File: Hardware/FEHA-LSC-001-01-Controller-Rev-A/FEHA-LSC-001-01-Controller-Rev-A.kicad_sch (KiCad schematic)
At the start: 0 parts

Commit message: LSC: project library parts, schematic capture in progress
Library (_FEHA-LSC-001):
- Imported SI2356DS-T1-GE3, TPS560430XFDBVR, FXL0420-100-M, HDGC4001SMD-S-2P from LCSC;
  ESP32-C3-MINI-1-H4X(4MB) copied from GeyserSense. Fields filled, pin types normalised,
  pins<->pads verified (buck and MOSFET pinouts checked against vendor PDFs)
- TPS560430 symbol pins rearranged by function (VIN/EN left, CB/SW/FB right, GND bottom)

Schematic: reverse-polarity stage, buck (51k/22k divider, 2x10uF 50V input) and MCU core
drawn; BOM fields (Mfr. Part #, LCSC Part #, Package) filled on all placed parts.
Field pass proven electrically neutral with design_diff.py.

Spec BOM: white status LED (C34499) and button (C720477), as GeyserSense.

Co-Authored-By: Claude Opus 5.5 <noreply@anthropic.com>
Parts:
- added C1, C6, C7: 100nF, PCM_JLCPCB:C_0402, symbol PCM_JLCPCB-Capacitors:0402,100nF
- added C2: 1uF, PCM_JLCPCB:C_0402, symbol PCM_JLCPCB-Capacitors:0402,1uF
- added C3, C8: 10uF, PCM_JLCPCB:C_1206, symbol PCM_JLCPCB-Capacitors:1206,10uF
- added C4: 10uF, PCM_JLCPCB:C_0603, symbol PCM_JLCPCB-Capacitors:0603,10uF,(2)
- added C5: 22uF, PCM_JLCPCB:C_1206, symbol PCM_JLCPCB-Capacitors:1206,22uF,(2)
- added CN1: HDGC4001SMD-S-2P, _FEHA-LSC-001:CONN-SMD_2P-P4.00_HDGC4001SMD-S-2P, symbol _FEHA-LSC-001:HDGC4001SMD-S-2P
- added D1: SS34, PCM_JLCPCB:D_SMA, symbol PCM_JLCPCB-Diodes:Schottky,SS34
- added D2: SMBJ26A, PCM_JLCPCB:D_SMB, symbol PCM_JLCPCB-Diodes:TVS-Uni,SMBJ26A
- added D3: White, PCM_JLCPCB:D_0805, symbol PCM_JLCPCB-Diodes:LED,0805,White
- added D4: B5819W SL, PCM_JLCPCB:D_SOD-123, symbol PCM_JLCPCB-Diodes:Schottky,B5819W SL
- added D5: BZT52C10, PCM_JLCPCB:D_SOD-123, symbol PCM_JLCPCB-Diodes:Zener,BZT52C10
- added L1: 10uH, _FEHA-LSC-001:IND-SMD_L4.4-W4.2, symbol _FEHA-LSC-001:FXL0420-100-M
- added Q1: HL2310A, PCM_JLCPCB:Q_SOT-23, symbol PCM_JLCPCB-Transistors:NMOS,HL2310A
- added R1, R2, R4, R8: 10kΩ, PCM_JLCPCB:R_0402, symbol PCM_JLCPCB-Resistors:0402,10kΩ
- added R3: 100kΩ, PCM_JLCPCB:R_0402, symbol PCM_JLCPCB-Resistors:0402,100kΩ
- added R5: 51kΩ, PCM_JLCPCB:R_0402, symbol PCM_JLCPCB-Resistors:0402,51kΩ
- added R6: 22kΩ, PCM_JLCPCB:R_0402, symbol PCM_JLCPCB-Resistors:0402,22kΩ
- added R7: 470Ω, PCM_JLCPCB:R_0402, symbol PCM_JLCPCB-Resistors:0402,470Ω
- added S1: Tactile Button, 160gf, PCM_JLCPCB:SW_TS-1088-AR02016, symbol PCM_JLCPCB-Connectors_Buttons:Tactile Button, 160gf, 12V, 50mA, 4.0mm
- added TP1: GND, TestPoint:TestPoint_Pad_D1.5mm, symbol Connector:TestPoint_Small
- added TP3: EN, TestPoint:TestPoint_Pad_D1.5mm, symbol Connector:TestPoint_Small
- added TP4: VIN, TestPoint:TestPoint_Pad_D1.5mm, symbol Connector:TestPoint_Small
- added U1: TPS560430XFDBVR, _FEHA-LSC-001:SOT-23-6_L2.9-W1.6-P0.95-LS2.8-BR, symbol _FEHA-LSC-001:TPS560430XFDBVR
- added U2: ESP32-C3-MINI-1-H4X(4MB), _FEHA-LSC-001:WIFIM-SMD_ESP32-C3-MINI-1, symbol _FEHA-LSC-001:ESP32-C3-MINI-1-H4X(4MB)
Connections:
- new net: C7.1, U1.1 (CB)
- new net: D3.2, R7.2
- new net +24V: C3.1, C8.1, CN1.1, D2.1, R3.1, U1.4 (EN), U1.5 (VIN)
- new net +3V3: C4.1, C5.1, C6.1, L1.1, R1.1, R2.1, R4.1, R5.1, R8.1, U2.3 (3V3)
- new net BTN: C1.1, R1.2, S1.1 (A), U2.23 (IO9)
- new net EN: C2.1, R8.2, TP3.1, U2.8 (EN)
- new net FB: R5.2, R6.1, U1.3 (FB)
- new net GND: C1.2, C2.2, C3.2, C4.2, C5.2, C6.2, C8.2, D2.2, D3.1, D5.2, Q1.2 (S), R6.2, S1.2 (B), TP1.1, U1.2 (GND), U2.1 (GND), U2.11 (GND), U2.14 (GND), U2.2 (GND), U2.36 (GND), U2.37 (GND), U2.38 (GND), U2.39 (GND), U2.40 (GND), U2.41 (GND), U2.42 (GND), U2.43 (GND), U2.44 (GND), U2.45 (GND), U2.46 (GND), U2.47 (GND), U2.48 (GND), U2.49 (GND), U2.50 (GND), U2.51 (GND), U2.52 (GND), U2.53 (GND)
- new net G_REV: D5.1, Q1.1 (G), R3.2
- new net IO2: R4.2, U2.5 (IO2)
- new net IO8: R2.2, U2.22 (IO8)
- new net LED_USER: R7.1, U2.16 (IO10)
- new net SW: C7.2, L1.2, U1.6 (SW)
- new net VBUS: D4.2
- new net VIN_N: CN1.2, Q1.3 (D)
- no-connect marks 0 -> 5
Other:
- note added: "Microprocessor"

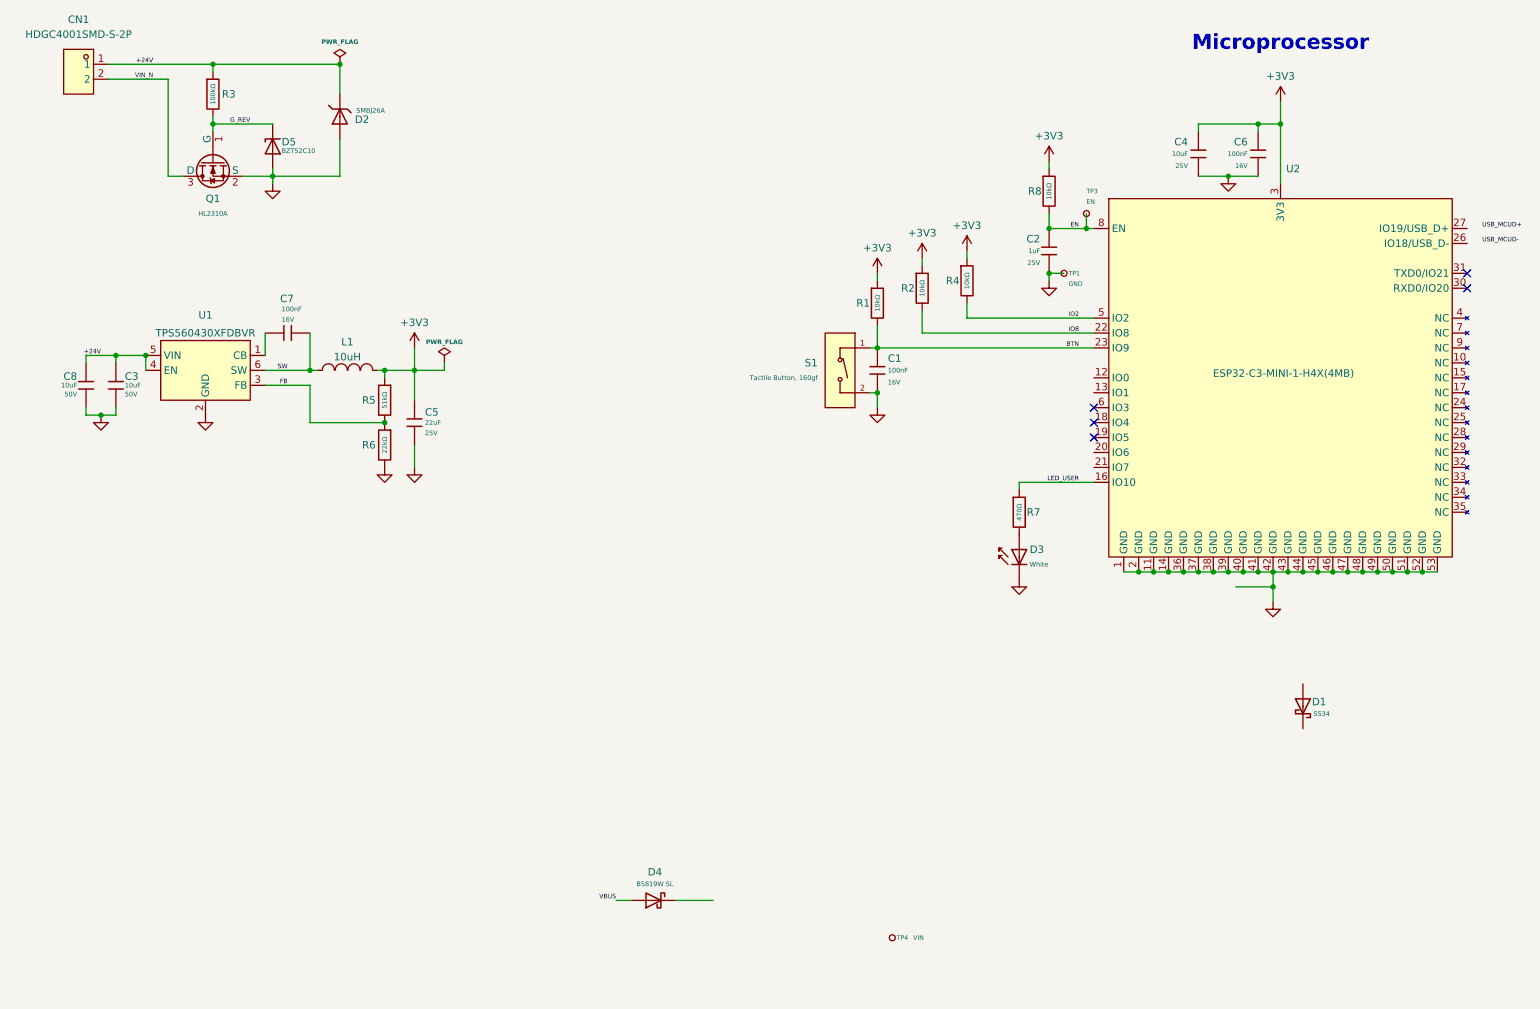
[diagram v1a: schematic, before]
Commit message: LSC: output stage, USB debug header, PWR_1A net class
- Output stage: SI2356DS low-side switch (100R gate series, 10k pull-down), SS34
  freewheel, 1uF 50V 0805 local bypass (C28323), drain test point TP6 + GND TP7
- CN3 USB debug header (VBUS, D-, D+, GND) on new locking footprint
  PinHeader_1x04_P2.54mm_Vertical_Lock (holes staggered +-0.127 mm for an unsoldered
  press-fit header); USB_MCUD+/- wired to U2 IO19/IO18
- Removed the two net-class flags carried over from GeyserSense; new net class PWR_1A
  (1.0 mm track) on /+24V, /VIN_N, /LED_N, GND (spec §7 rule 6)
- BOM fields filled on C10 and R10; flag removal proven neutral with design_diff.py.
  ERC clean apart from kicad-cli library-path warnings

Co-Authored-By: Claude Opus 5.5 <noreply@anthropic.com>
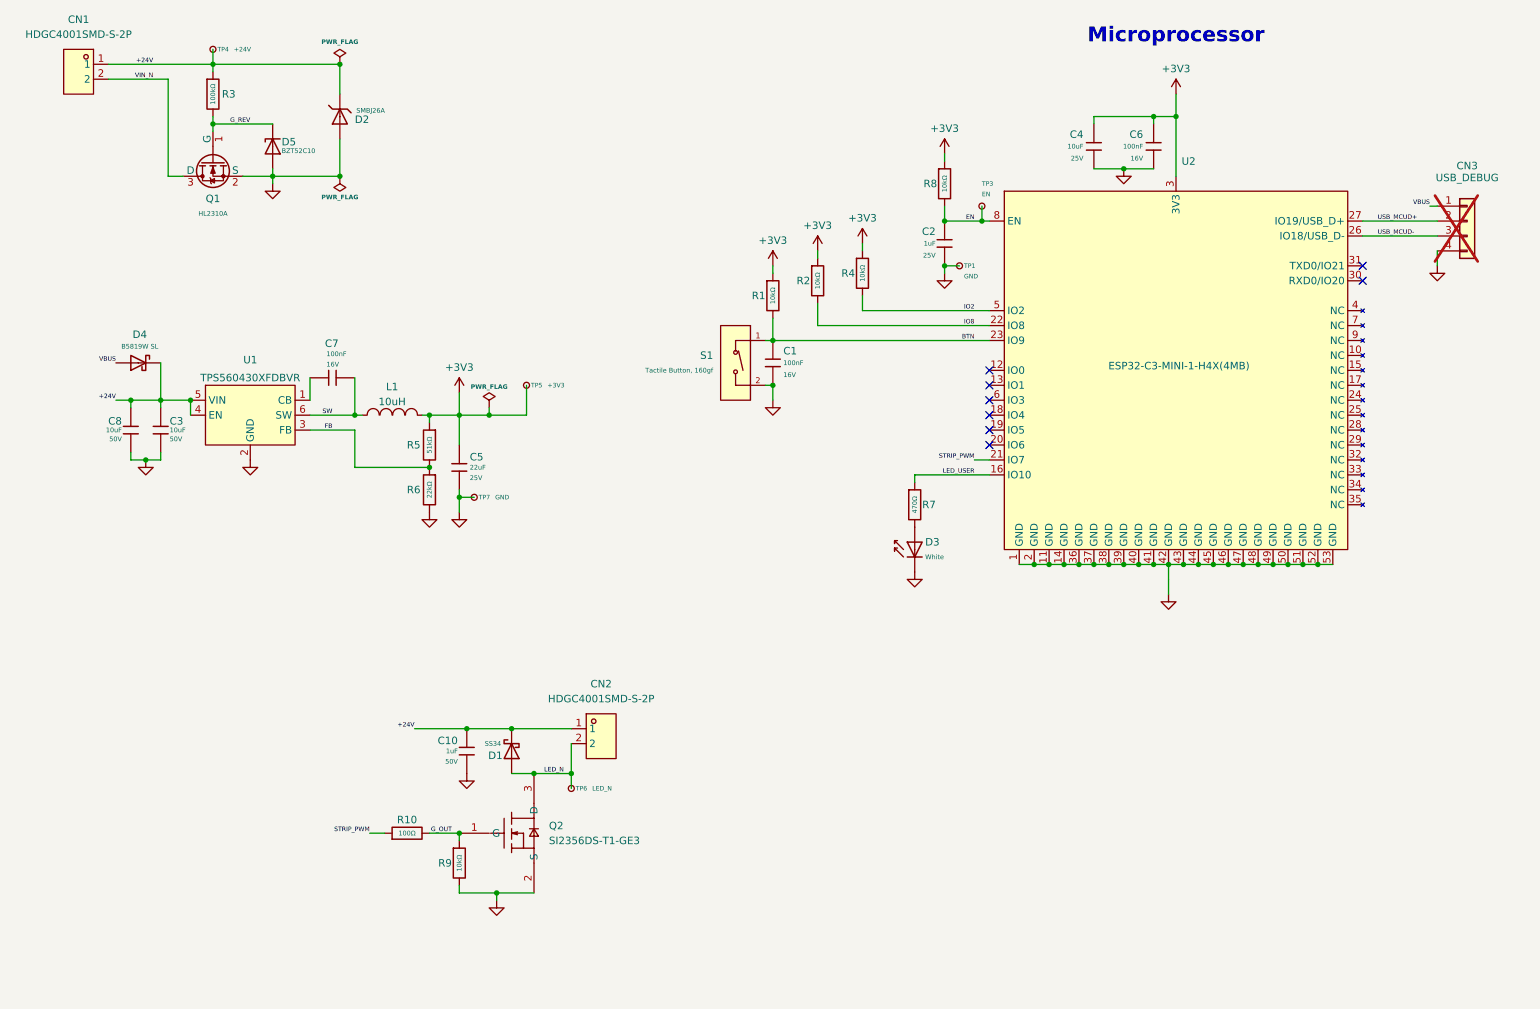
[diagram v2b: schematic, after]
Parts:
- added C10: 1uF, PCM_JLCPCB:C_0805, symbol PCM_JLCPCB-Capacitors:0805,1uF
- added CN2: HDGC4001SMD-S-2P, _FEHA-LSC-001:CONN-SMD_2P-P4.00_HDGC4001SMD-S-2P, symbol _FEHA-LSC-001:HDGC4001SMD-S-2P
- added CN3: USB_DEBUG, _FEHA-LSC-001:PinHeader_1x04_P2.54mm_Vertical_Lock, symbol Connector_Generic:Conn_01x04
- added Q2: SI2356DS-T1-GE3, _FEHA-LSC-001:SOT-23_L2.9-W1.3-P1.90-LS2.4-BR, symbol _FEHA-LSC-001:SI2356DS-T1-GE3
- added R10: 100Ω, PCM_JLCPCB:R_0402, symbol PCM_JLCPCB-Resistors:0402,100Ω
- added R9: 10kΩ, PCM_JLCPCB:R_0402, symbol PCM_JLCPCB-Resistors:0402,10kΩ
- added TP5: +3V3, TestPoint:TestPoint_Pad_D1.5mm, symbol Connector:TestPoint_Small
- added TP6: LED_N, TestPoint:TestPoint_Pad_D1.5mm, symbol Connector:TestPoint_Small
- added TP7: GND, TestPoint:TestPoint_Pad_D1.5mm, symbol Connector:TestPoint_Small
- TP4: value VIN -> +24V
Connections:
- net +24V: now also D1.1, D4.1, TP4.1, C10.1, CN2.1
- net +3V3: now also TP5.1
- net GND: now also C10.2, CN3.4 (Pin_4), Q2.2 (S), R9.2, TP7.1
- net USB_MCUD+: now also U2.27 (IO19/USB_D+), CN3.2 (Pin_2)
- net USB_MCUD-: now also U2.26 (IO18/USB_D-), CN3.3 (Pin_3)
- net VBUS: now also CN3.1 (Pin_1)
- net STRIP_PWM: now reaches U2.21 (IO7)
- net STRIP_PWM: now also R10.1
- net LED_N: now reaches D1.2
- net LED_N: now also CN2.2, Q2.3 (D), TP6.1
- new net G_OUT: Q2.1 (G), R10.2, R9.1
- no-connect marks 5 -> 8
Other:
- moved on the sheet: C1, C2, C3, C4, C5, C6, C7, C8, D1, D3, D4, L1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

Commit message: LSC CHG-01: 100 nF 50 V HF bypass at buck input (review PWR-3)
Add C9 (C307331, 100 nF 50 V X7R 0402) across +24V/GND at U1 VIN per
TPS560430 §9.2.2.6. C1, C6, C7 moved to the same part, so all 100 nF
positions are one BOM line. House sourcing fields restored after the
Change Symbol pass. Netlist otherwise unchanged; ERC 0 errors.

Adds the schematic-gate review register (2026-10-02); PWR-3 closed,
FUNC-7 and three Minors open.

Co-Authored-By: Claude Opus 5.5 <noreply@anthropic.com>
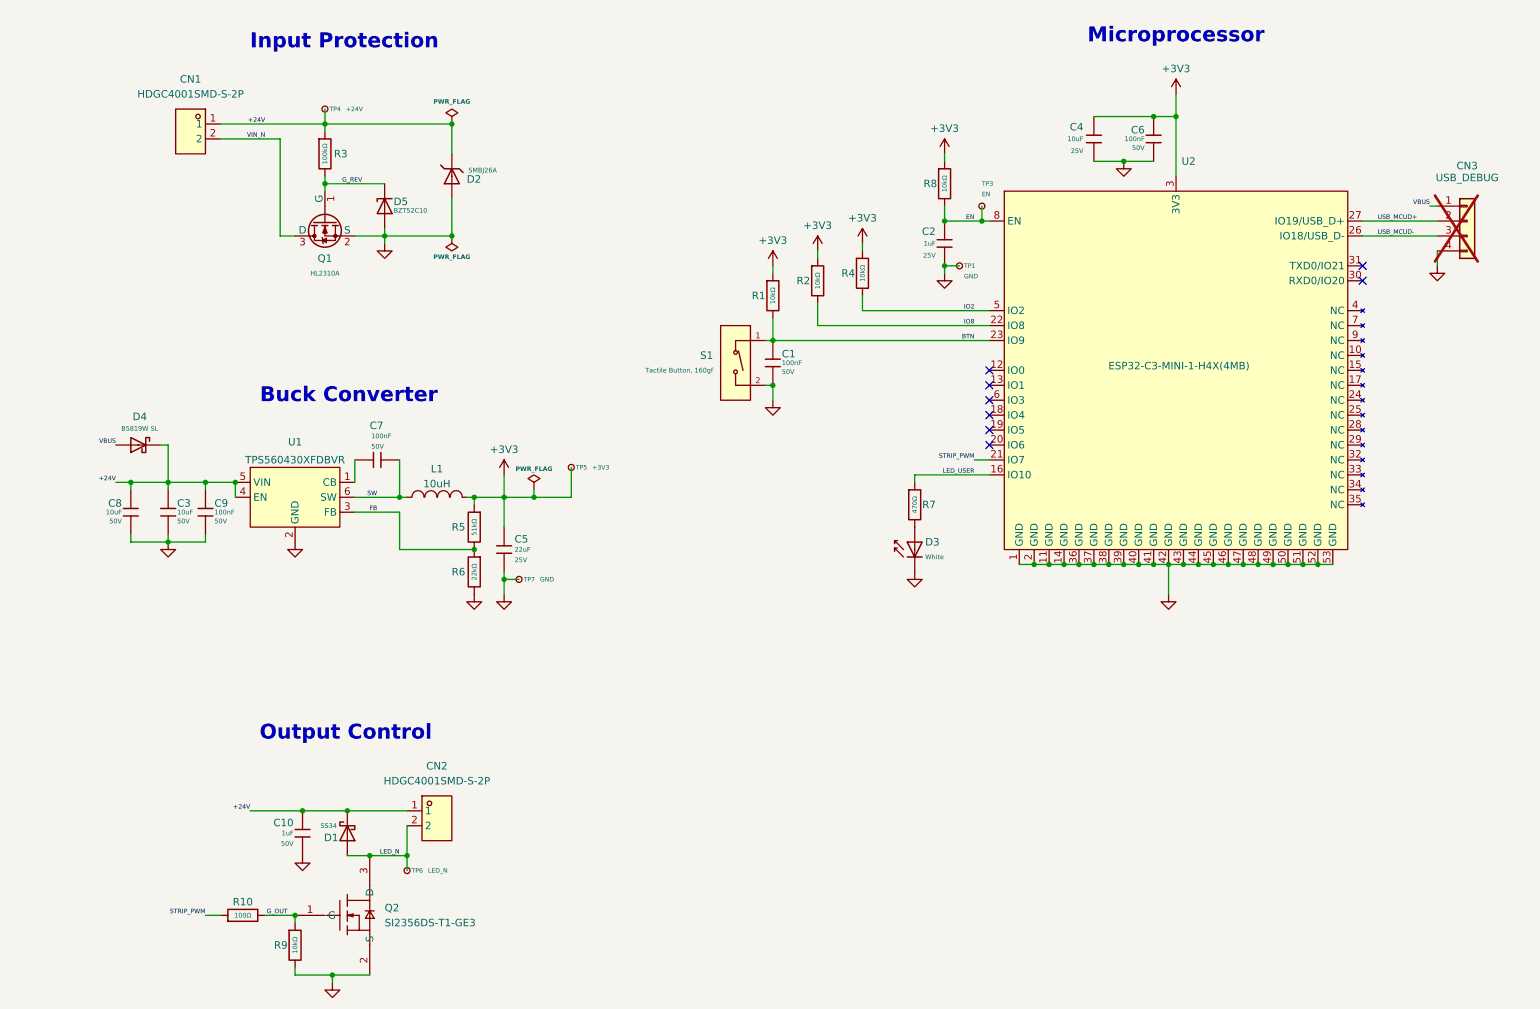
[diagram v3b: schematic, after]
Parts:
- removed C1, C6: 100nF, PCM_JLCPCB:C_0402, symbol PCM_JLCPCB-Capacitors:0402,100nF
- added C1, C6, C9: 100nF, PCM_JLCPCB:C_0402, symbol PCM_JLCPCB-Capacitors:0402,100nF,(2)
- C7: LCSC C1525 -> C307331; LCSC Part # C1525 -> C307331; Mfr. Part # CL05B104KO5NNNC -> CL05B104KB54PNC; Part CL05B104KO5NNNC -> CL05B104KB54PNC; Price 0.004USD -> 0.008USD; Stock 20208285 -> 8389599; Voltage Rated 16V -> 50V
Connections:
- net +24V: now also C9.1
- net +3V3: now also C6.1
- net BTN: now also C1.1
- net GND: now also C1.2, C6.2, C9.2
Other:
- note added: "Buck Converter"
- note added: "Input Protection"
- note added: "Output Control"
- moved on the sheet: C10, C3, C4, C5, C7, C8, CN1, CN2, D1, D2, D4, D5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

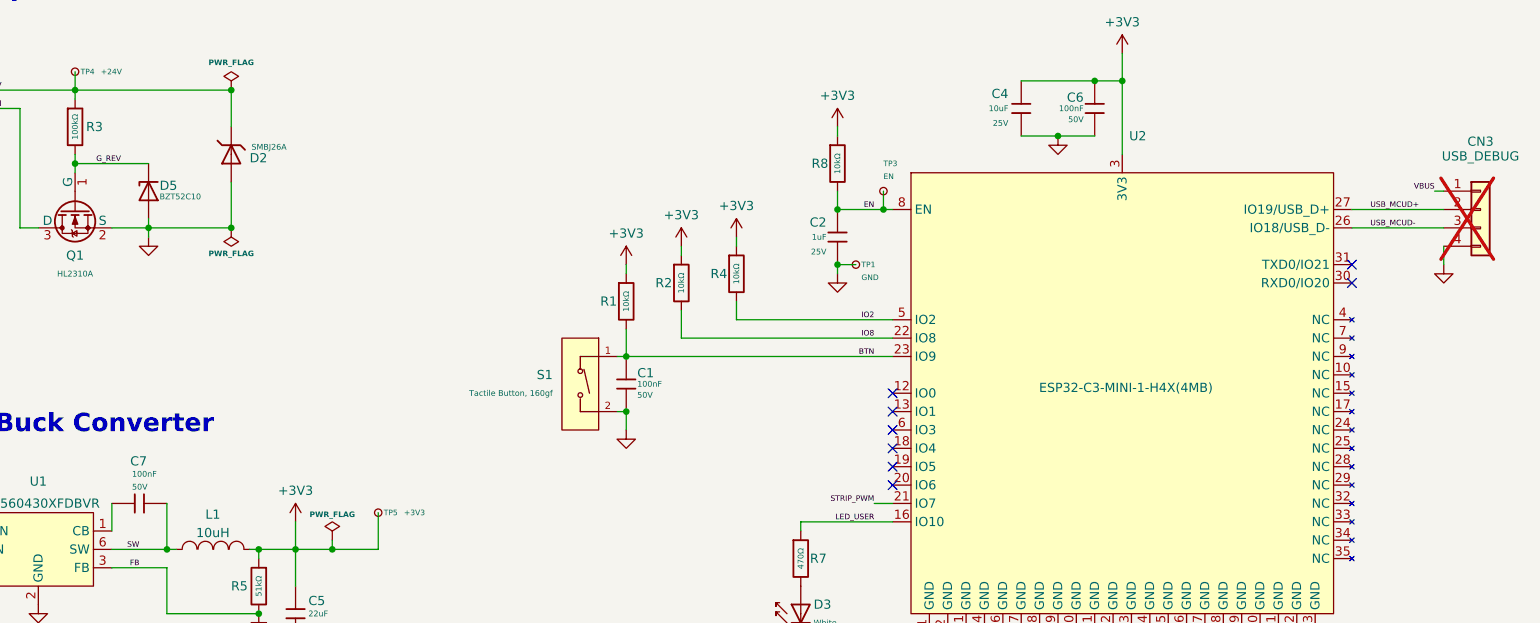
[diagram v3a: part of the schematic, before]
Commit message: LSC CHG-02: debug header in standard USB pin order (review FUNC-7)
CN3 pins 2/3 swapped to 5V, D-, D+, GND to mate with the stock bench
pigtail; spec §6 states the order. C7 relinked to the 50 V 100 nF
library entry (CHG-01 follow-up, fields unchanged).

Review PART-5 accepted: R7 stays 470 ohm (same white LED visible at
1 kohm on FEHA-RM-001 Rev A); recorded in spec §9 and as a profile
deferral. Netlist: only the two USB data nets changed; ERC 0 errors.

Co-Authored-By: Claude Opus 5.5 <noreply@anthropic.com>
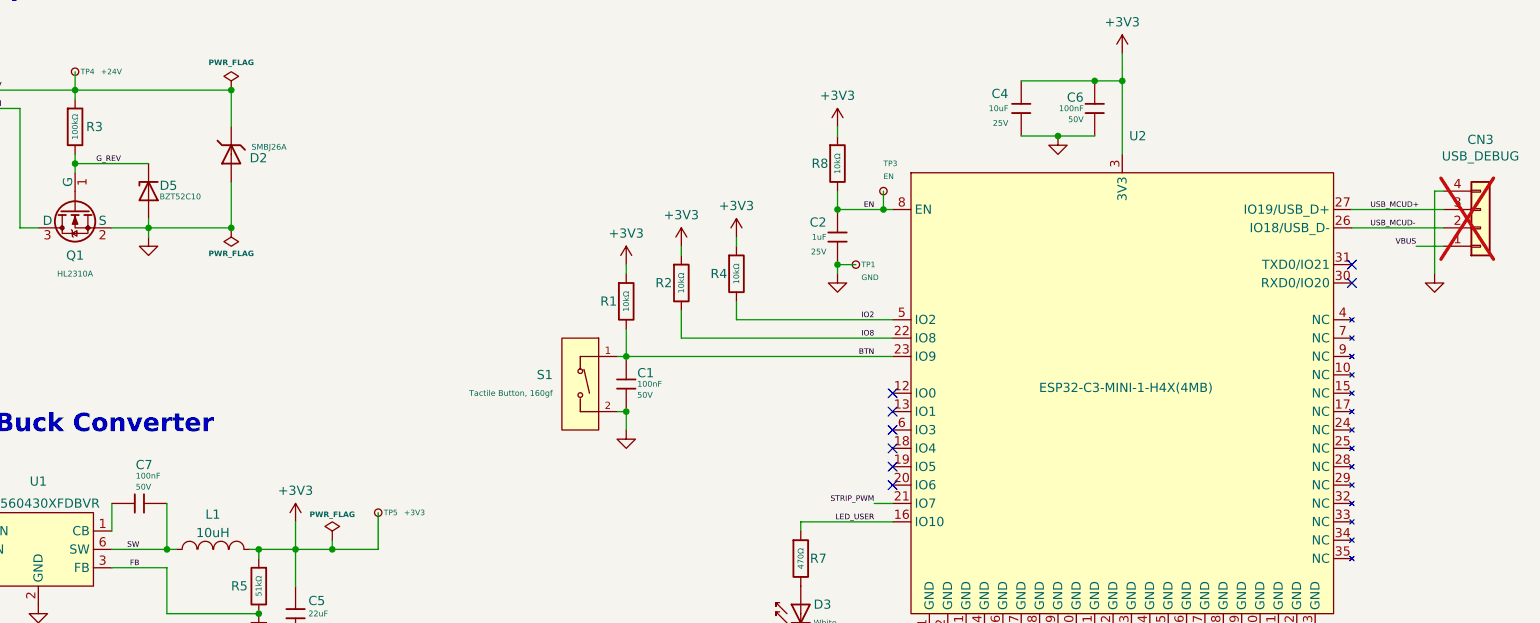
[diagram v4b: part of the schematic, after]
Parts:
- removed C7: 100nF, PCM_JLCPCB:C_0402, symbol PCM_JLCPCB-Capacitors:0402,100nF
- added C7: 100nF, PCM_JLCPCB:C_0402, symbol PCM_JLCPCB-Capacitors:0402,100nF,(2)
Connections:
- net SW: now also C7.2
- net USB_MCUD+: now also CN3.3 (Pin_3); no longer CN3.2 (Pin_2)
- net USB_MCUD-: now also CN3.2 (Pin_2); no longer CN3.3 (Pin_3)
- net at U1.1 (CB): now also C7.1
